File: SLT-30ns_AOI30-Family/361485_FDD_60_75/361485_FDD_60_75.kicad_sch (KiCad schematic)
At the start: 9 parts, among them U1 12-Pin_SLx_Can

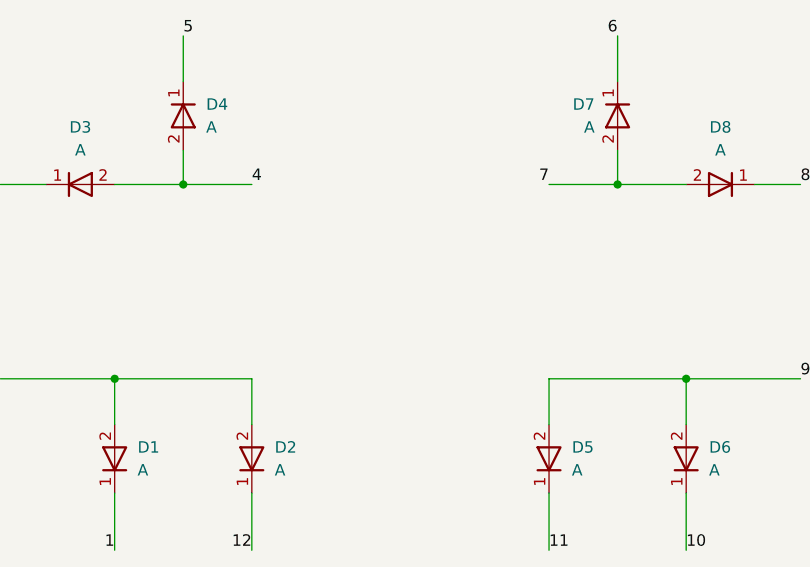
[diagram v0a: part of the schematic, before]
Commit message: Update schematic pdfs
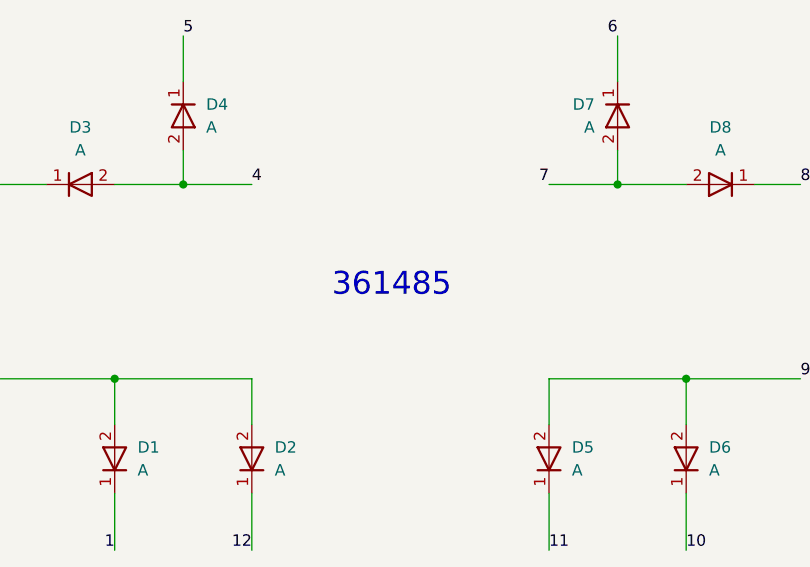
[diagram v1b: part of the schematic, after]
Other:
- note added: "361485"
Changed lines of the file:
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@@
     (stroke (width 0) (type default) (color 0 0 0 0))
+  )
+  (text "361485" (at 113.03 92.71 0)
+    (effects (font (size 2.54 2.54)) (justify left bottom))
   )
   (text "All Diodes A" (at 113.03 57.15 0)
